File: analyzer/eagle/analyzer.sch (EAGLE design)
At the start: 34 parts, among them J3 USBSMD, U1 ATA6631, U2 FT232RL, U3 ATMEGA328, X1 16MHz

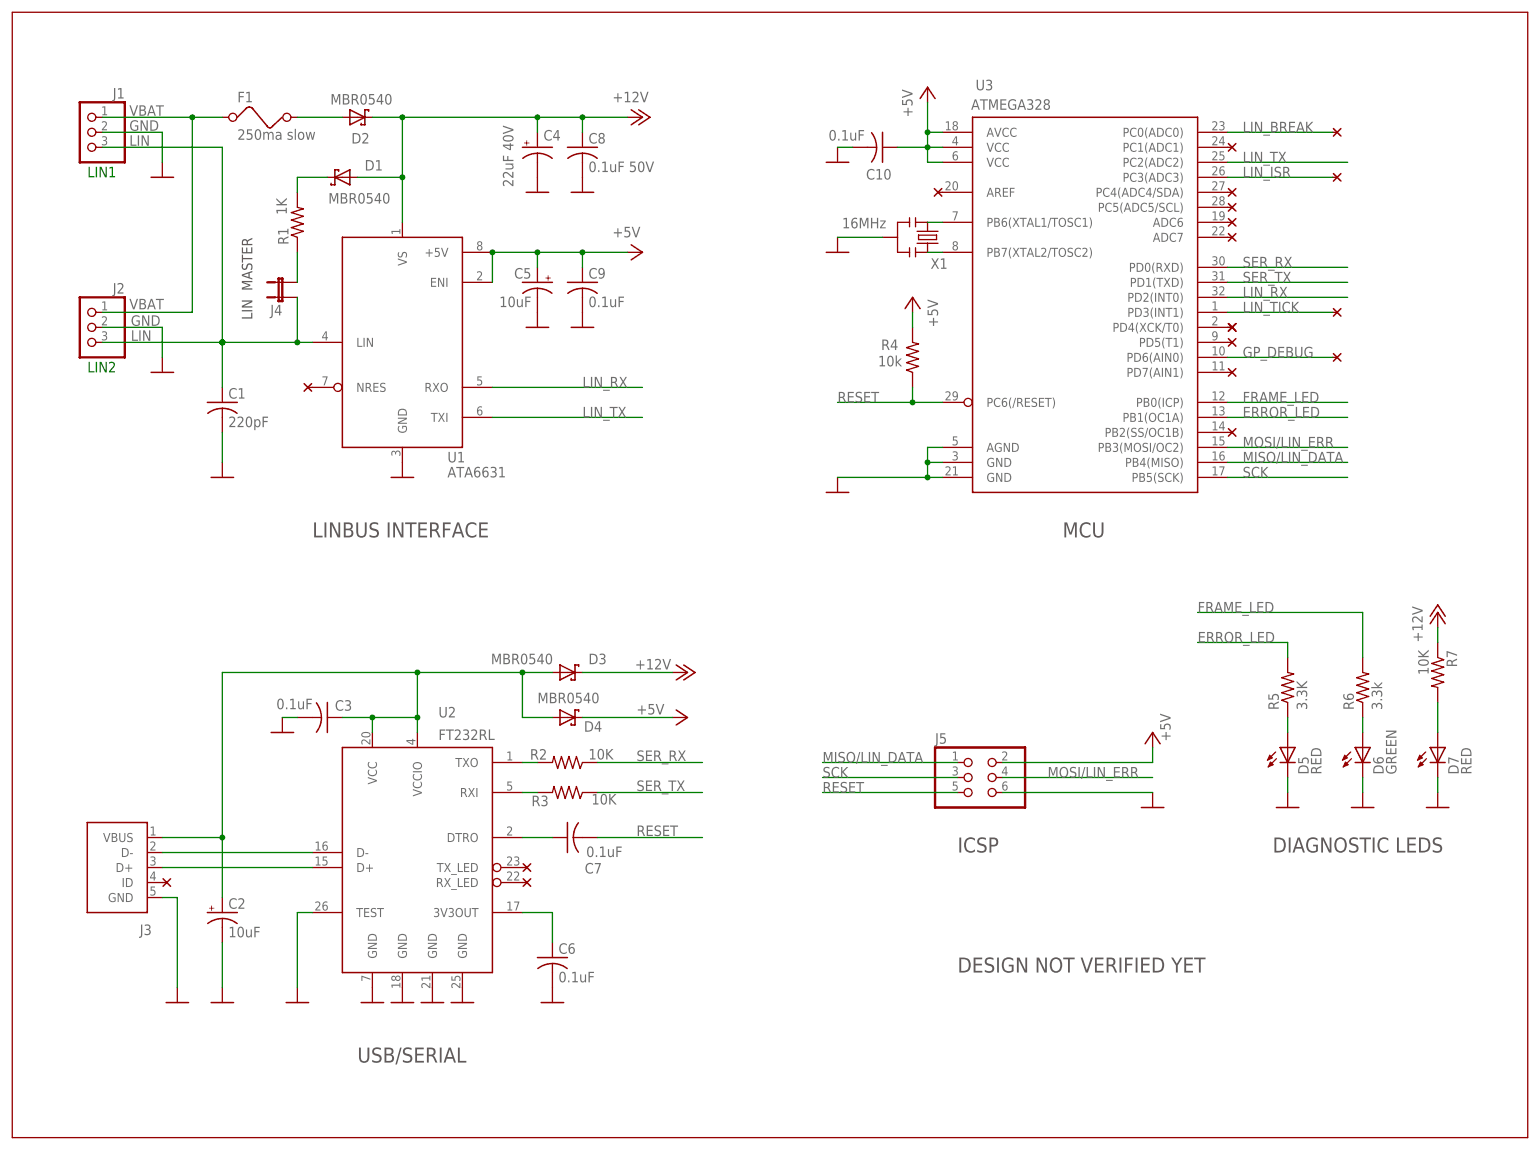
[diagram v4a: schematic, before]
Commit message: Added Analyzer bom.
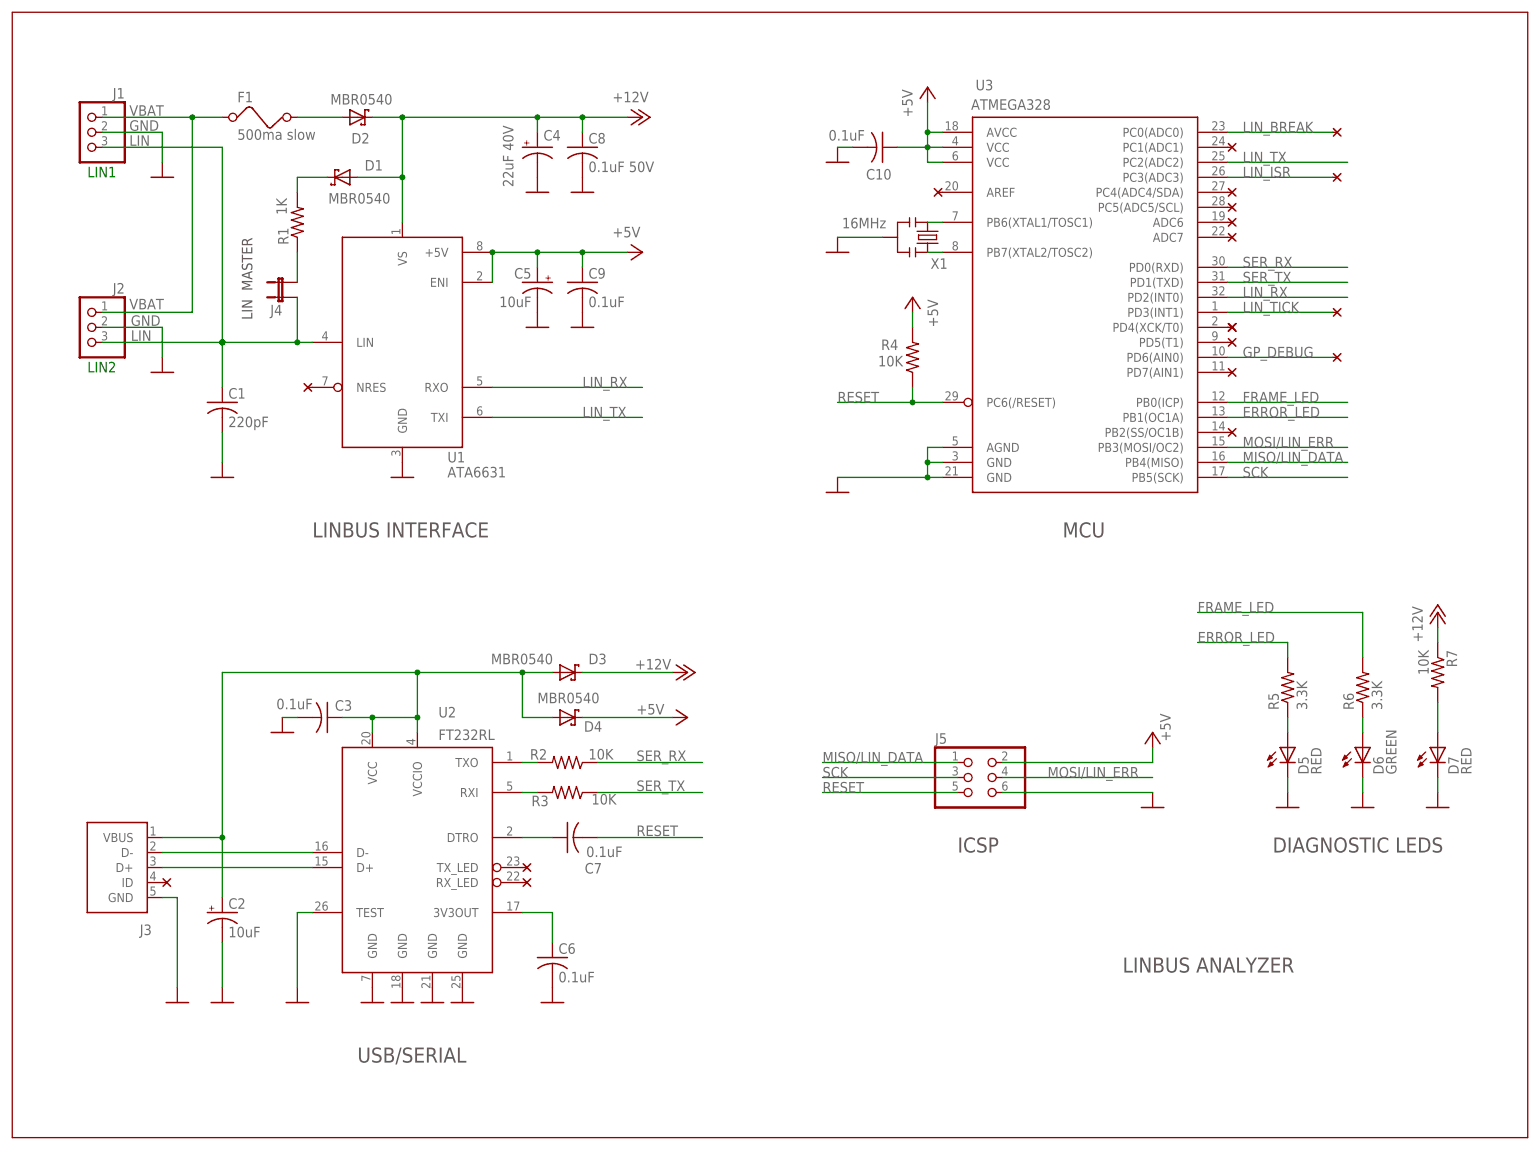
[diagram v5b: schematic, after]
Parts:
- F1: value 250ma slow -> 500ma slow
- R4: value 10k -> 10K
- R6: value 3.3k -> 3.3K
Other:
- note added: "LINBUS ANALYZER"
- note removed: "DESIGN NOT VERIFIED YET"
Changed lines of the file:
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@@
 <parts>
 <part name="R5" library="analyzer" deviceset="R-US_" device="R0805" value="3.3K"/>
-<part name="R6" library="analyzer" deviceset="R-US_" device="R0805" value="3.3k"/>
+<part name="R6" library="analyzer" deviceset="R-US_" device="R0805" value="3.3K"/>
 <part name="C1" library="analyzer" deviceset="C-US" device="C0805" value="220pF"/>
 <part name="J1" library="analyzer" deviceset="PINHD-1X3" device=""/>
@@
 <part name="C4" library="analyzer" deviceset="CPOL-US" device="UD-6,3X5,8" value="22uF 40V"/>
 <part name="C8" library="analyzer" deviceset="C-US" device="C0805" value="0.1uF 50V"/>
-<part name="F1" library="analyzer" deviceset="FUSE" device="" value="250ma slow"/>
+<part name="F1" library="analyzer" deviceset="FUSE" device="" value="500ma slow"/>
 <part name="C5" library="analyzer" deviceset="CPOL-US" device="A/3216-18R" value="10uF"/>
-<part name="R4" library="analyzer" deviceset="R-US_" device="R0805" value="10k"/>
+<part name="R4" library="analyzer" deviceset="R-US_" device="R0805" value="10K"/>
 <part name="P+1" library="analyzer" deviceset="+5V" device=""/>
 <part name="C10" library="analyzer" deviceset="C-US" device="C0805" value="0.1uF"/>
@@
 <text x="213.36" y="73.66" size="2.54" layer="97">ICSP</text>
 <text x="231.14" y="127" size="2.54" layer="97">MCU</text>
-<text x="213.36" y="53.34" size="2.54" layer="97" font="vector">DESIGN NOT VERIFIED YET</text>
+<text x="241.3" y="53.34" size="2.54" layer="97" font="vector">LINBUS ANALYZER</text>
 <text x="266.7" y="73.66" size="2.54" layer="97">DIAGNOSTIC LEDS</text>
 <wire x1="53.34" y1="215.9" x2="309.88" y2="215.9" width="0.1524" layer="94"/>

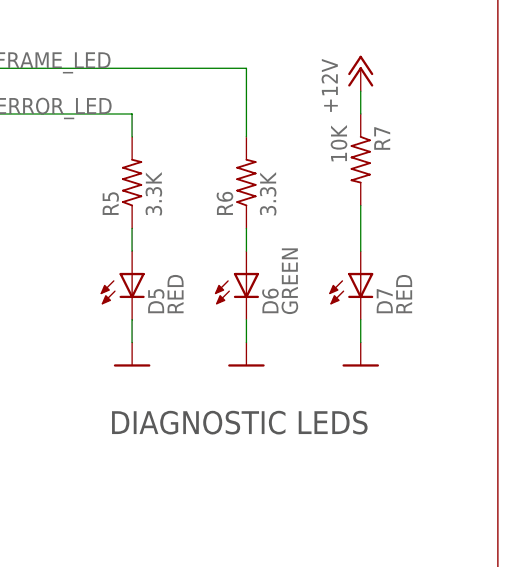
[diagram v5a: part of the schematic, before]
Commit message: Harmonized the design of the three boards. Changed the beepr configuration button sequence (ignition on, 6 clicks, ignition off).
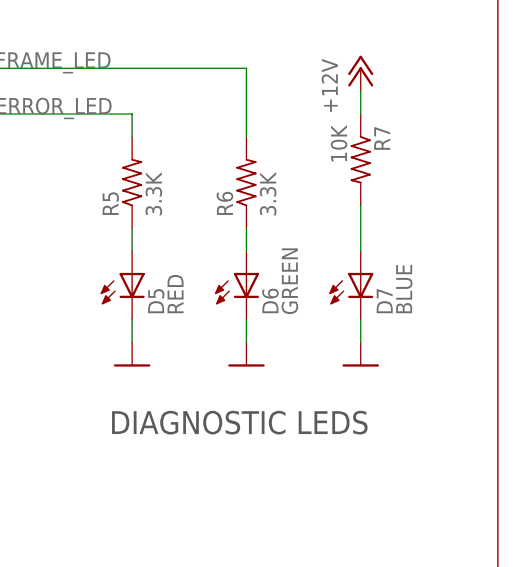
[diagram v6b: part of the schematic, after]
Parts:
- D7: value RED -> BLUE
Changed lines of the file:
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@@
 <part name="C2" library="analyzer" deviceset="CPOL-US" device="A/3216-18R" value="10uF"/>
 <part name="GND1" library="analyzer" deviceset="GND" device=""/>
-<part name="D7" library="analyzer" deviceset="LED" device="" value="RED"/>
+<part name="D7" library="analyzer" deviceset="LED" device="" value="BLUE"/>
 <part name="R7" library="analyzer" deviceset="R-US_" device="R0805" value="10K"/>
 <part name="P+4" library="analyzer" deviceset="+5V" device=""/>
